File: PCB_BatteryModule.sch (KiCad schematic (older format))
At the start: 47 parts, among them J1 Interconnect A, J2 Interconnect B, J3 Debug, J4 Conn_01x04, Q1 IRF7406, Q2 IRF7469, U1 LM22679-5.0, U2 ACS712, U3 XMC1404_F064, U4 TLE7251, U5 LM35-D, U6 LM35-D

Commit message: Use AA Ni-Mh cells instead of 18650 Li-ion
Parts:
- removed D2: LED, PCB_BatteryModule:C_0805_HandSoldering, symbol Device:LED
- removed F1: Fuse, PCB_BatteryModule:Keystone_3557_Fuse_Holder, symbol Device:Fuse
- removed J4: Conn_01x04, PCB_BatteryModule:WAGO_2604-1104_PCB_Terminal_Block_4-Way, symbol Connector_Generic:Conn_01x04
- removed Q2: IRF7469, Package_SO:SOIC-8_3.9x4.9mm_P1.27mm, symbol Transistor_FET:IRF7403
- removed R7: 1K2, PCB_BatteryModule:C_0805_HandSoldering, symbol Device:R
- added BT4, BT5: AA, PCB_BatteryModule:Battery_AA_THT_Keystone_590, symbol Device:Battery_Cell
- added C20: 4.7uF, PCB_BatteryModule:C_0805_HandSoldering, symbol Device:CP_Small
- added C21, C22: 0.1uF, PCB_BatteryModule:C_0805_HandSoldering, symbol Device:C_Small
- added C23: 47uF, Capacitor_Tantalum_SMD:CP_EIA-7343-43_Kemet-X_Pad2.25x2.55mm_HandSolder, symbol Device:CP_Small
- added C24: 0.01uF, PCB_BatteryModule:C_0805_HandSoldering, symbol Device:C_Small
- added C25: 0.33uF, PCB_BatteryModule:C_0805_HandSoldering, symbol Device:C_Small
- added J4: Button/Status, Connector_PinHeader_2.54mm:PinHeader_2x05_P2.54mm_Horizontal, symbol Connector_Generic:Conn_02x05_Odd_Even
- added J5: Barrel_Jack, Connector_BarrelJack:BarrelJack_CUI_PJ-036AH-SMT_Horizontal, symbol Connector:Barrel_Jack
- added L2: 47uH, PCB_BatteryModule:Inductor_SMD_Bourns_SRR1280, symbol Device:L_Small
- added Q2: IRF7303, Package_SO:SOIC-8_3.9x4.9mm_P1.27mm, symbol irf7303ipbf:IRF7303IPBF
- added Q3: IRF7303, Package_SO:SOIC-8_3.9x4.9mm_P1.27mm, symbol Transistor_FET:IRF7309IPBF
- added Q4: IRF7309, Package_SO:SOIC-8_3.9x4.9mm_P1.27mm, symbol Transistor_FET:IRF7309IPBF
- added R10: 68K, PCB_BatteryModule:C_0805_HandSoldering, symbol Device:R
- added R11: 0.1, PCB_BatteryModule:C_2010_5025Metric_HandSoldering, symbol Device:R
- added R12: 850K, PCB_BatteryModule:C_0805_HandSoldering, symbol Device:R
- added R13: 100K, PCB_BatteryModule:C_0805_HandSoldering, symbol Device:R
- added U7: MAX1640, Package_SO:SOIC-16_3.9x9.9mm_P1.27mm, symbol BatteryModule:MAX1640
- added U8: ULN2003A, Package_SO:SOIC-16_3.9x9.9mm_P1.27mm, symbol Transistor_Array:ULN2003A
- BT1, BT2, BT3: value 18650 -> AA; footprint PCB_BatteryModule:BatteryContact_THT_Keystone_590 -> PCB_BatteryModule:Battery_AA_THT_Keystone_590
- C6: footprint Capacitors_Tantalum_SMD:CP_Tantalum_Case-X_EIA-7343-43_Hand -> Capacitor_Tantalum_SMD:CP_EIA-7343-43_Kemet-X_Pad2.25x2.55mm_HandSolder
- R2, R3: value 2K -> 380K
- R5: value 18K -> 23K3
- R6: value 18K -> 200K
- U2: value ACS712 -> MCS1803GS-05P
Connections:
- net +5V: now also J4.3 (Pin_3), J4.5 (Pin_5), J4.7 (Pin_7)
- net +BATT: now also BT1.1 (+), Q1.1 (S), Q1.2 (S), Q1.3 (S), R4.1, R8.2, J4.10 (Pin_10), R11.2, R12.1, U7.10 (CS-); no longer C1.1, C2.1, C3.1, J1.3 (Pin_3), J2.3 (Pin_3), U1.2 (VIN), U2.3 (IP-), U2.4 (IP-)
- net -BATT: now also R5.1, BT5.2 (-), C20.2, C21.2, C22.1, C23.2, C24.1, J4.1 (Pin_1), J4.2 (Pin_2), J5.2, Q2.1 (S), Q2.3 (1), Q3.1 (S), Q4.1 (S), R10.1, R13.2, U7.12 (PGND), U7.9 (GND), U8.8 (GND); no longer BT3.2 (-)
- net MAIN_POWER_ON: now also R2.1, Q2.4 (G); no longer R9.1
- net at BT1.2 (-), BT2.1 (+): no longer R5.1
- net at BT2.2 (-), BT3.1 (+): no longer R6.1
- net CHG_D0: now reaches U3.28 (P1.6)
- net CHG_D0: now also U7.4 (D0)
- net CHG_D1: now reaches U3.29 (P1.5)
- net CHG_D1: now also U7.3 (D1)
- net BUTTON: now reaches U3.4 (P4.7)
- net BUTTON: now also Q3.7 (D), Q3.8 (D)
- net STATUS_RGB_RED: now reaches U3.60 (P4.1)
- net STATUS_RGB_RED: now also U8.1 (I1)
- net STATUS_RGB_GREEN: now reaches U3.61 (P4.2)
- net STATUS_RGB_GREEN: now also U8.2 (I2)
- net STATUS_RGB_BLUE: now reaches U3.62 (P4.3)
- net STATUS_RGB_BLUE: now also U8.3 (I3)
- net at Q1.4 (G), R8.1: now also Q2.5 (D), Q2.6 (D), Q2.7 (D), Q2.8 (D)
- net STATUS_LED: no longer names the net of U3.8 (P4.11)
- removed net V_BAT2: R2.1, R5.2, U3.19 (P2.10)
- removed net V_BAT3: R3.1, R6.2, U3.20 (P2.11)
- new net: BT3.2 (-), BT4.1 (+)
- new net: J4.9 (Pin_9), Q2.2 (G), Q3.2 (G), R3.1, R9.1
- new net: BT4.2 (-), BT5.1 (+)
- new net: C20.1, C21.1, U7.1 (LDOL)
- new net: L2.2, R11.1, U7.11 (CS+)
- new net: Q4.2 (G), U7.13 (NDRV)
- new net: Q4.4 (G), U7.14 (PDRV)
- new net: C25.2, U7.15 (LDOH)
- new net: C23.1, C25.1, J5.1, Q4.5 (D), Q4.6 (D), U7.16 (IN)
- new net: R5.2, U7.2 (TOFF)
- new net: C24.2, U7.5 (CC)
- new net: C22.2, R6.2, U7.6 (REF)
- new net: R10.2, R6.1, U7.7 (SET)
- new net: R12.2, R13.1, U7.8 (TERM)
- new net: L2.1, Q4.3 (1), Q4.7 (D), Q4.8 (D)
- new net STATUS_RGB_BLUE_C: J4.8 (Pin_8), U8.14 (O3)
- new net STATUS_RGB_GREEN_C: J4.6 (Pin_6), U8.15 (O2)
- new net STATUS_RGB_RED_C: J4.4 (Pin_4), U8.16 (O1)
- new net VDC: C1.1, C2.1, C3.1, J1.3 (Pin_3), J2.3 (Pin_3), U1.2 (VIN), U2.3 (IP-), U2.4 (IP-)
- no-connect marks 1 -> 10
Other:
- note removed: "TODO:\n - USE IRF9393 INSTEAD OF IRF7406\n - VERIFY CAN\n - VERIFY TEMP"
- moved on the sheet: BT1, BT2, BT3, C1, C10, C11, C12, C13, C14, C15, C16, C17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

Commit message: Version 2.0 with a lot of improvements
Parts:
- added D2, D3, D4: LED, LED_SMD:LED_0805_2012Metric_Pad1.15x1.40mm_HandSolder, symbol Device:LED
- added R14, R15, R7: 10K, PCB_BatteryModule:C_0805_HandSoldering, symbol Device:R
- added R16: 18K, PCB_BatteryModule:C_0805_HandSoldering, symbol Device:R
- added R17: 2K, PCB_BatteryModule:C_0805_HandSoldering, symbol Device:R
- added SW1: SW_Push, Button_Switch_SMD:SW_SPST_Omron_B3FS-100xP, symbol Switch:SW_Push
- U1: footprint TO_SOT_Packages_SMD:TO-263-7_TabPin8 -> Package_TO_SOT_SMD:TO-263-7_TabPin8
- U7: footprint Package_SO:SOIC-16_3.9x9.9mm_P1.27mm -> Package_SO:QSOP-16_3.9x4.9mm_P0.635mm
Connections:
- net +5V: now also J4.4 (Pin_4), J4.6 (Pin_6), J4.8 (Pin_8), D2.2 (A), D3.2 (A), D4.2 (A); no longer J4.3 (Pin_3), J4.5 (Pin_5), J4.7 (Pin_7)
- net +BATT: now also SW1.1
- net -BATT: now also R17.2
- net STATUS_RGB_BLUE_C: now also J4.3 (Pin_3), R15.1; no longer J4.8 (Pin_8)
- net STATUS_RGB_GREEN_C: now also J4.5 (Pin_5), R14.1; no longer J4.6 (Pin_6)
- net STATUS_RGB_RED_C: now also J4.7 (Pin_7), R7.1; no longer J4.4 (Pin_4)
- net CHARGER_CONNECTED: now reaches U3.30 (P1.4)
- net CHARGER_CONNECTED: now also R16.2, R17.1
- net at J4.9 (Pin_9), Q2.2 (G), Q3.2 (G)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: now also SW1.2
- net at C23.1, C25.1, J5.1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: now also R16.1
- new net: D2.1 (K), R7.2
- new net: D3.1 (K), R14.2
- new net: D4.1 (K), R15.2
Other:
- moved on the sheet: C1, C10, C11, C12, C13, C14, C15, C2, C3, C4, C5, C6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

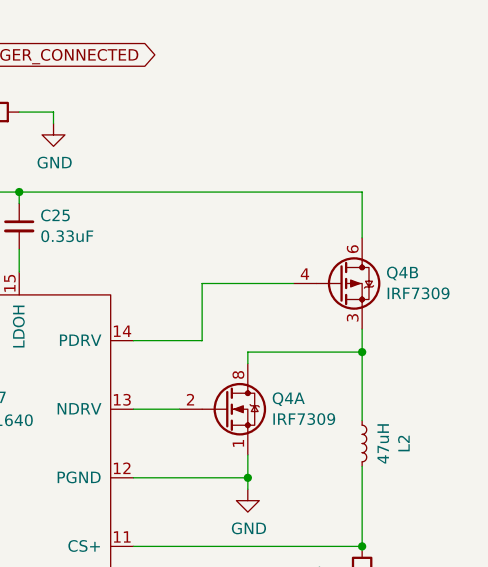
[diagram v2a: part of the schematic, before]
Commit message: Fix bug in the charger circuit where the P-channel mosfet was connected mirrored
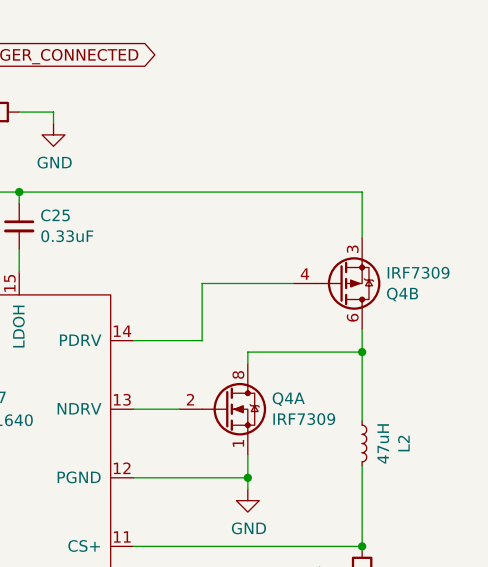
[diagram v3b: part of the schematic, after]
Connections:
- net at C23.1, C25.1, J5.1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: now also Q4.3 (1); no longer Q4.5 (D), Q4.6 (D)
- net at L2.1, Q4.7 (D), Q4.8 (D): now also Q4.5 (D), Q4.6 (D); no longer Q4.3 (1)
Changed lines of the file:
@@
-$EndComp
-$Comp
-L Transistor_FET:IRF7309IPBF Q4
-U 1 1 627C58D5
-P 14550 7550
-F 0 "Q4" H 14755 7596 50  0000 L CNN
-F 1 "IRF7309" H 14755 7505 50  0000 L CNN
-F 2 "Package_SO:SOIC-8_3.9x4.9mm_P1.27mm" H 14750 7475 50  0001 L CNN
-F 3 "http://www.irf.com/product-info/datasheets/data/irf7309ipbf.pdf" H 14650 7550 50  0001 L CNN
-	1    14550 7550
-	1    0    0    -1
-$EndComp
-$Comp
-L Transistor_FET:IRF7309IPBF Q4
-U 2 1 627C6398
-P 15050 7000
-F 0 "Q4" H 15255 7046 50  0000 L CNN
-F 1 "IRF7309" H 15255 6955 50  0000 L CNN
-F 2 "Package_SO:SOIC-8_3.9x4.9mm_P1.27mm" H 15250 6925 50  0001 L CNN
-F 3 "http://www.irf.com/product-info/datasheets/data/irf7309ipbf.pdf" H 15150 7000 50  0001 L CNN
-	2    15050 7000
-	1    0    0    -1
 $EndComp
 $Comp
@@
 Wire Wire Line
 	13250 6000 13250 6250
+$Comp
+L Transistor_FET:IRF7309IPBF Q4
+U 1 1 627C58D5
+P 14550 7550
+F 0 "Q4" H 14755 7596 50  0000 L CNN
+F 1 "IRF7309" H 14755 7505 50  0000 L CNN
+F 2 "Package_SO:SOIC-8_3.9x4.9mm_P1.27mm" H 14750 7475 50  0001 L CNN
+F 3 "http://www.irf.com/product-info/datasheets/data/irf7309ipbf.pdf" H 14650 7550 50  0001 L CNN
+	1    14550 7550
+	1    0    0    -1
+$EndComp
+$Comp
+L Transistor_FET:IRF7309IPBF Q4
+U 2 1 627C6398
+P 15050 7000
+F 0 "Q4" H 15255 7046 50  0000 L CNN
+F 1 "IRF7309" H 15255 6955 50  0000 L CNN
+F 2 "Package_SO:SOIC-8_3.9x4.9mm_P1.27mm" H 15250 6925 50  0001 L CNN
+F 3 "http://www.irf.com/product-info/datasheets/data/irf7309ipbf.pdf" H 15150 7000 50  0001 L CNN
+	2    15050 7000
+	1    0    0    1
+$EndComp
 $EndSCHEMATC
